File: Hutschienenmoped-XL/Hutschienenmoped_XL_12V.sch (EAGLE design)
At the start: 126 parts, among them J1 638207222005, J13 638207222005, J15 638207222008, J2 645004114822, J4 61300421121, J7 638207222005, J8 638207222007, U4 TLE9250VSJ

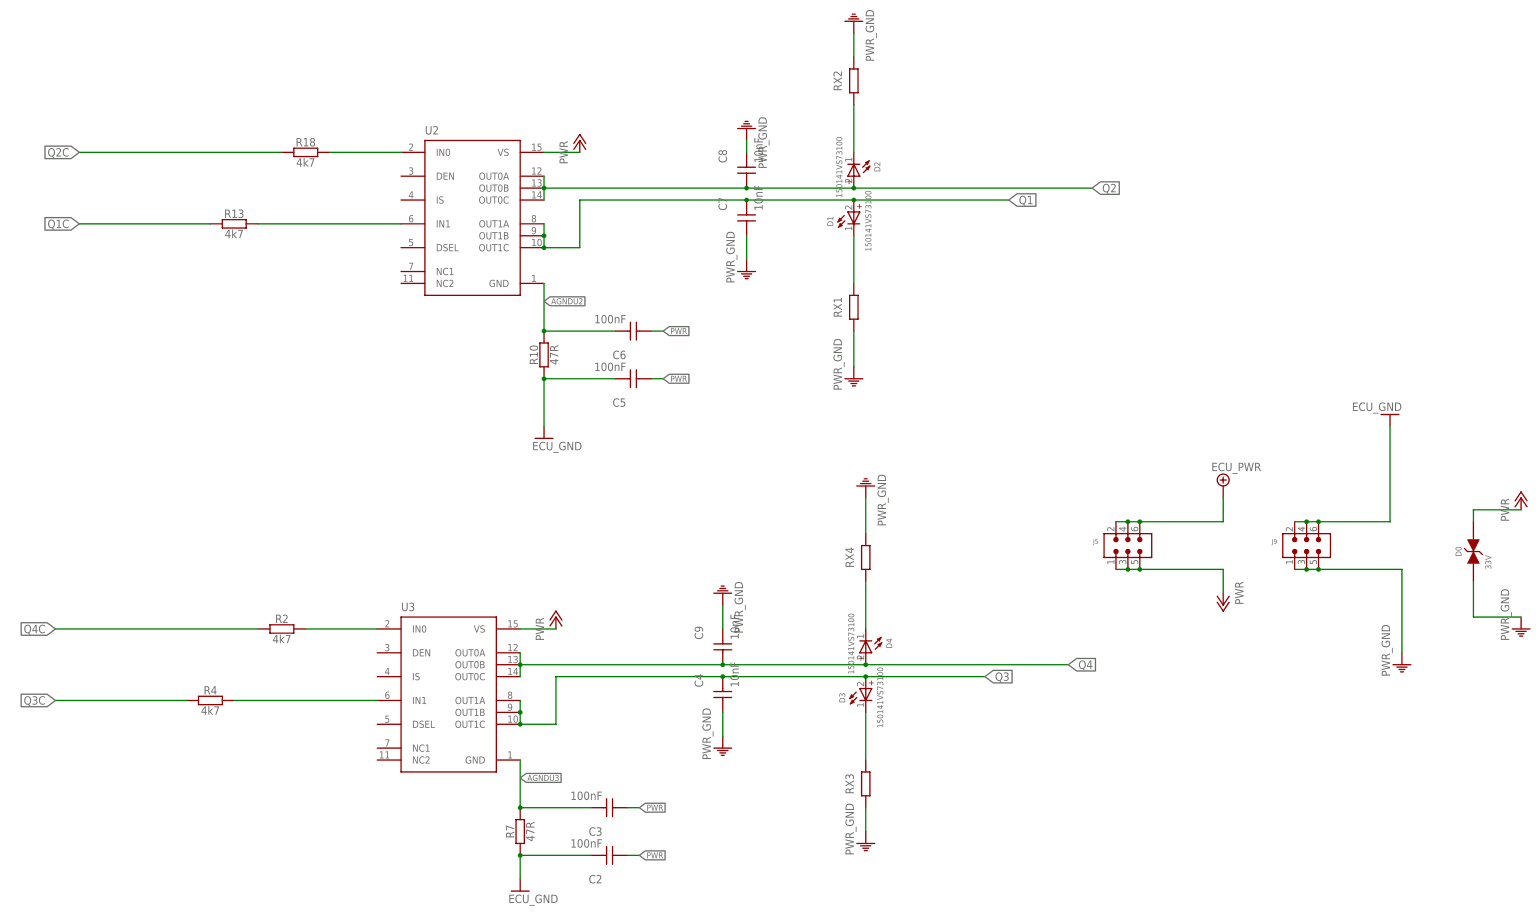
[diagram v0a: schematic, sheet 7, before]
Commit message: gitflow-feature-stash: prot Add SMA_DO-214AC package, elements D014 to D023 with attributes, and resistors R35 to R38. Update classes Ampere7 and clearance values. Include wire connections for new elements in signals Q3, Q1C, Q1, AGNDU3, and 5V.
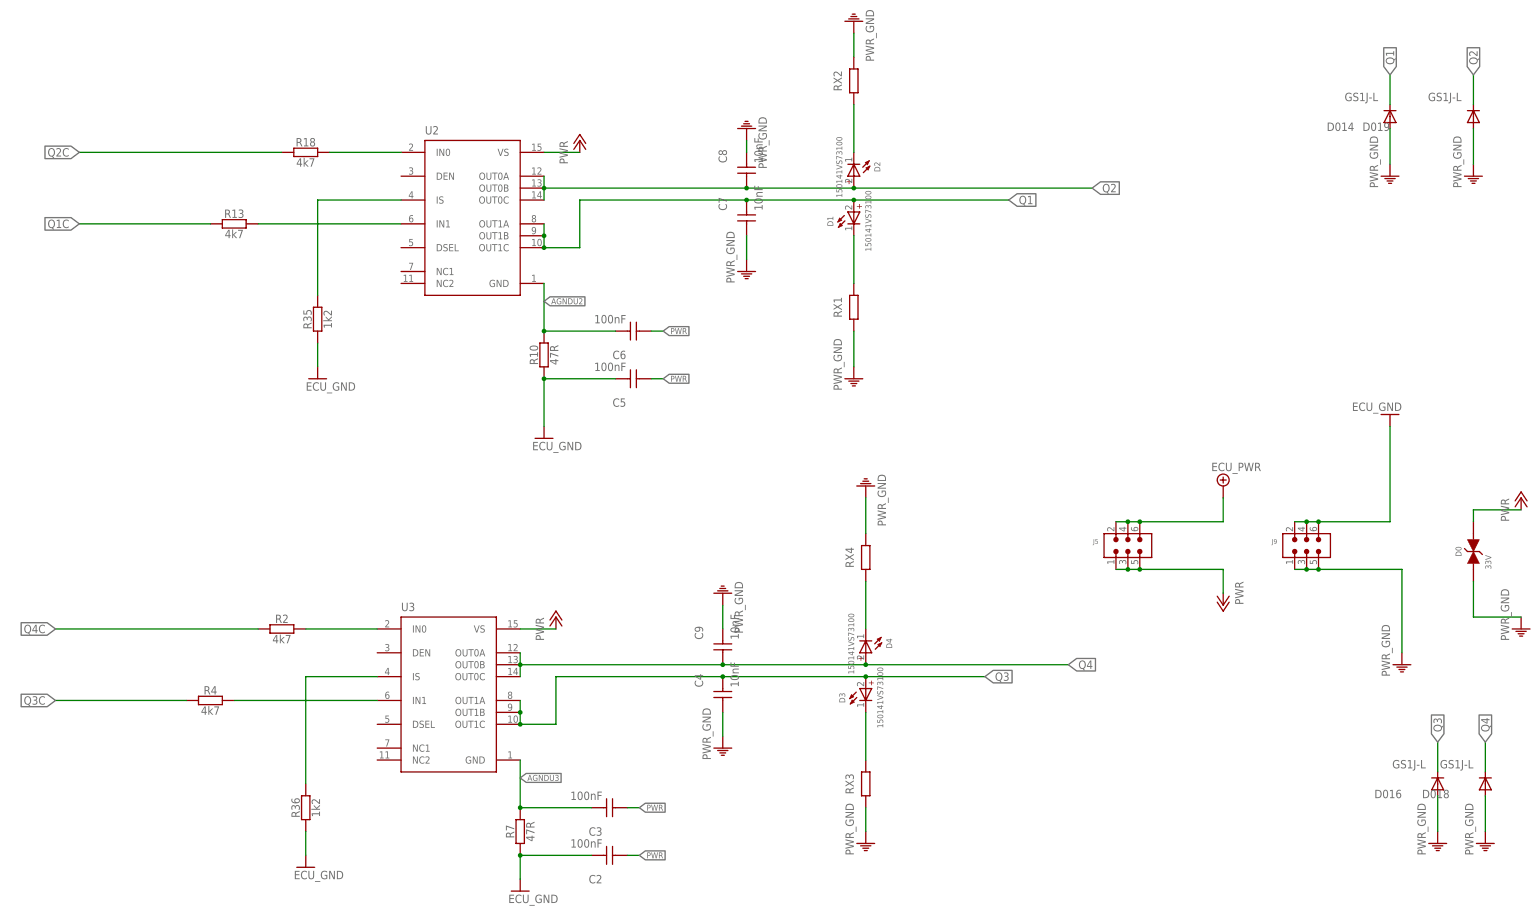
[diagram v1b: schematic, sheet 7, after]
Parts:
- added D014, D016, D018, D019, D020, D021, D022, D023: GS1J-L, fliegl-elektronik:GS1J-L
- added R35, R36, R37, R38: 1k2, resistor:R-EU_R0805
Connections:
- new net N$16: R38.2, U6.IS
- new net N$20: R35.2, U2.IS
- new net N$21: R36.2, U3.IS
- new net N$7: R37.2, U5.IS
- net ECU_GND: now also R35.1, R36.1, R37.1, R38.1
- net PWR_GND: now also D014.A, D016.A, D018.A, D019.A, D020.A, D021.A, D022.A, D023.A
- net Q1: now also D014.C
- net Q2: now also D019.C
- net Q3: now also D016.C
- net Q4: now also D018.C
- net Q5: now also D020.C
- net Q6: now also D021.C
- net Q7: now also D022.C
- net Q8: now also D023.C
